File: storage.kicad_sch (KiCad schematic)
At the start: 3 parts, among them J5 Micro_SD_Card_Det1, U1 MIMX8MM6DVTLZAA, U15 W25Q32JVZP

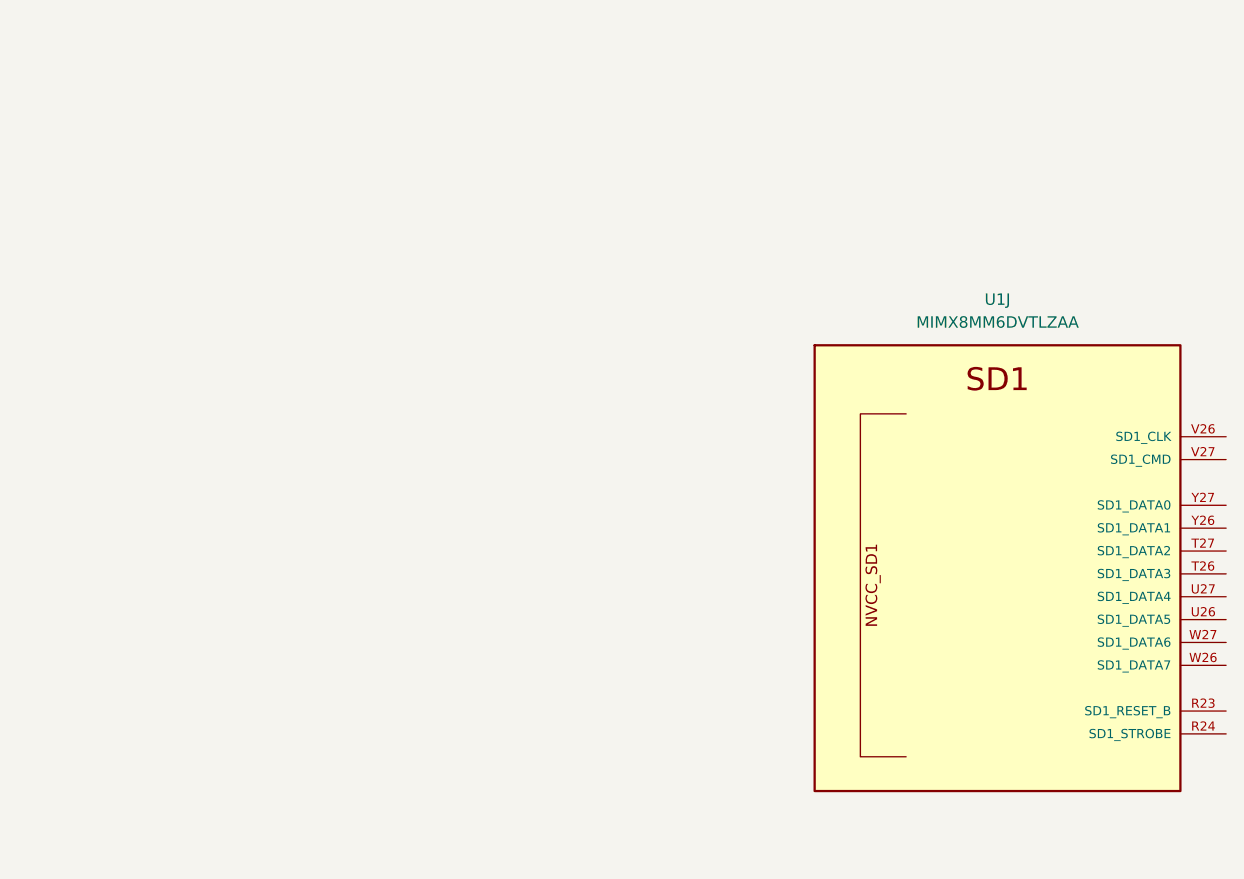
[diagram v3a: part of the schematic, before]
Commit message: enet sch done, other misc sch work
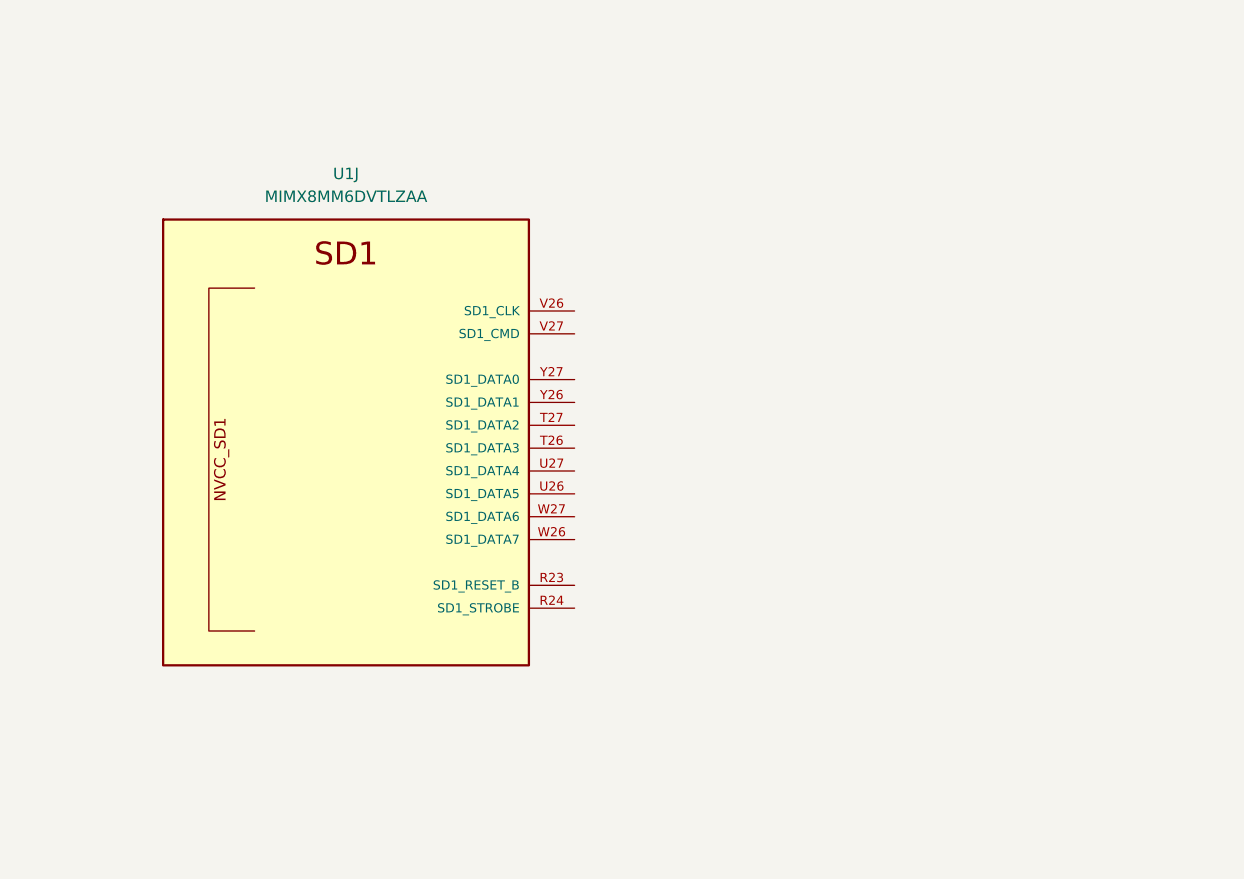
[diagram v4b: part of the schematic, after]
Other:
- moved on the sheet: U1J
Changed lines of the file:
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@@
     (pin "9")
   )
-  (symbol (lib_id "qsbc:MIMX8MM6DVTLZAA") (at 360.68 203.2 0) (unit 10)
+  (symbol (lib_id "qsbc:MIMX8MM6DVTLZAA") (at 288.29 189.23 0) (unit 10)
     (in_bom yes) (on_board yes) (fields_autoplaced)
-    (property "Reference" "U1" (id 0) (at 360.68 184.15 0))
-    (property "Value" "MIMX8MM6DVTLZAA" (id 1) (at 360.68 186.69 0))
-    (property "Footprint" "qsbc:SOT1967-1" (id 2) (at 364.49 393.7 0)
+    (property "Reference" "U1" (id 0) (at 288.29 170.18 0))
+    (property "Value" "MIMX8MM6DVTLZAA" (id 1) (at 288.29 172.72 0))
+    (property "Footprint" "qsbc:SOT1967-1" (id 2) (at 292.1 379.73 0)
       (effects (font (size 1.27 1.27)) (justify left bottom) hide)
     )
-    (property "Datasheet" "https://www.nxp.com/docs/en/data-sheet/IMX8MMCEC.pdf" (id 3) (at 361.95 397.51 0)
+    (property "Datasheet" "https://www.nxp.com/docs/en/data-sheet/IMX8MMCEC.pdf" (id 3) (at 289.56 383.54 0)
       (effects (font (size 1.27 1.27)) (justify left bottom) hide)
     )

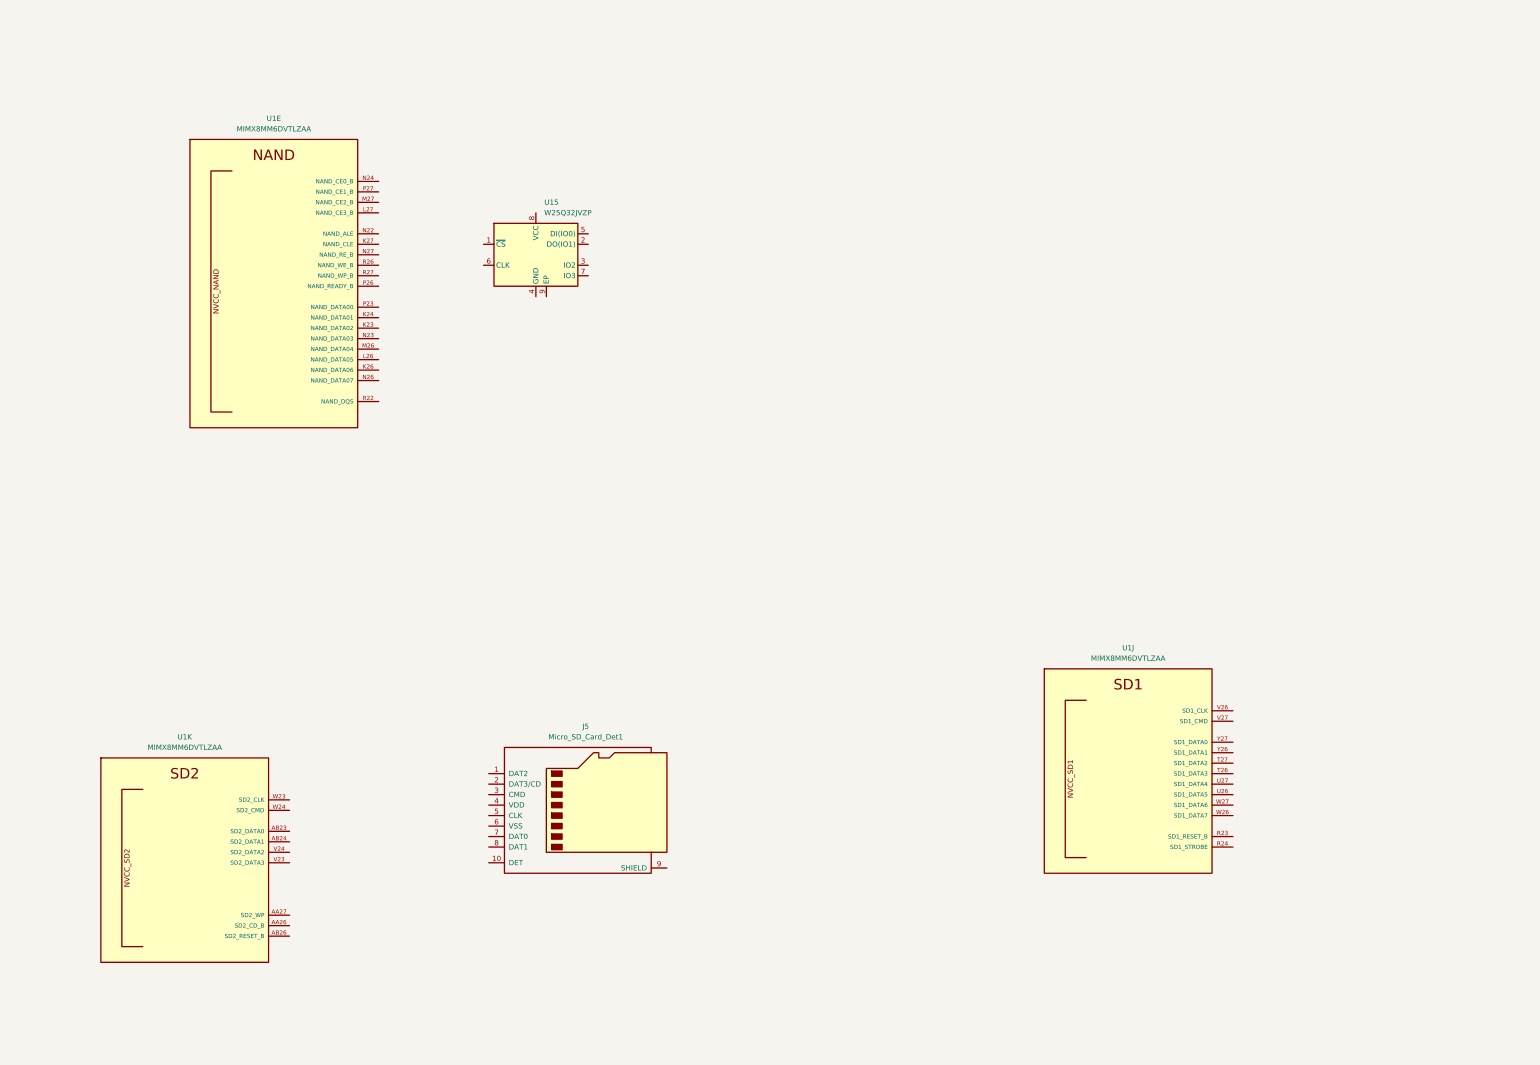
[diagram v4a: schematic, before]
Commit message: storage done, peri work, misc fixes
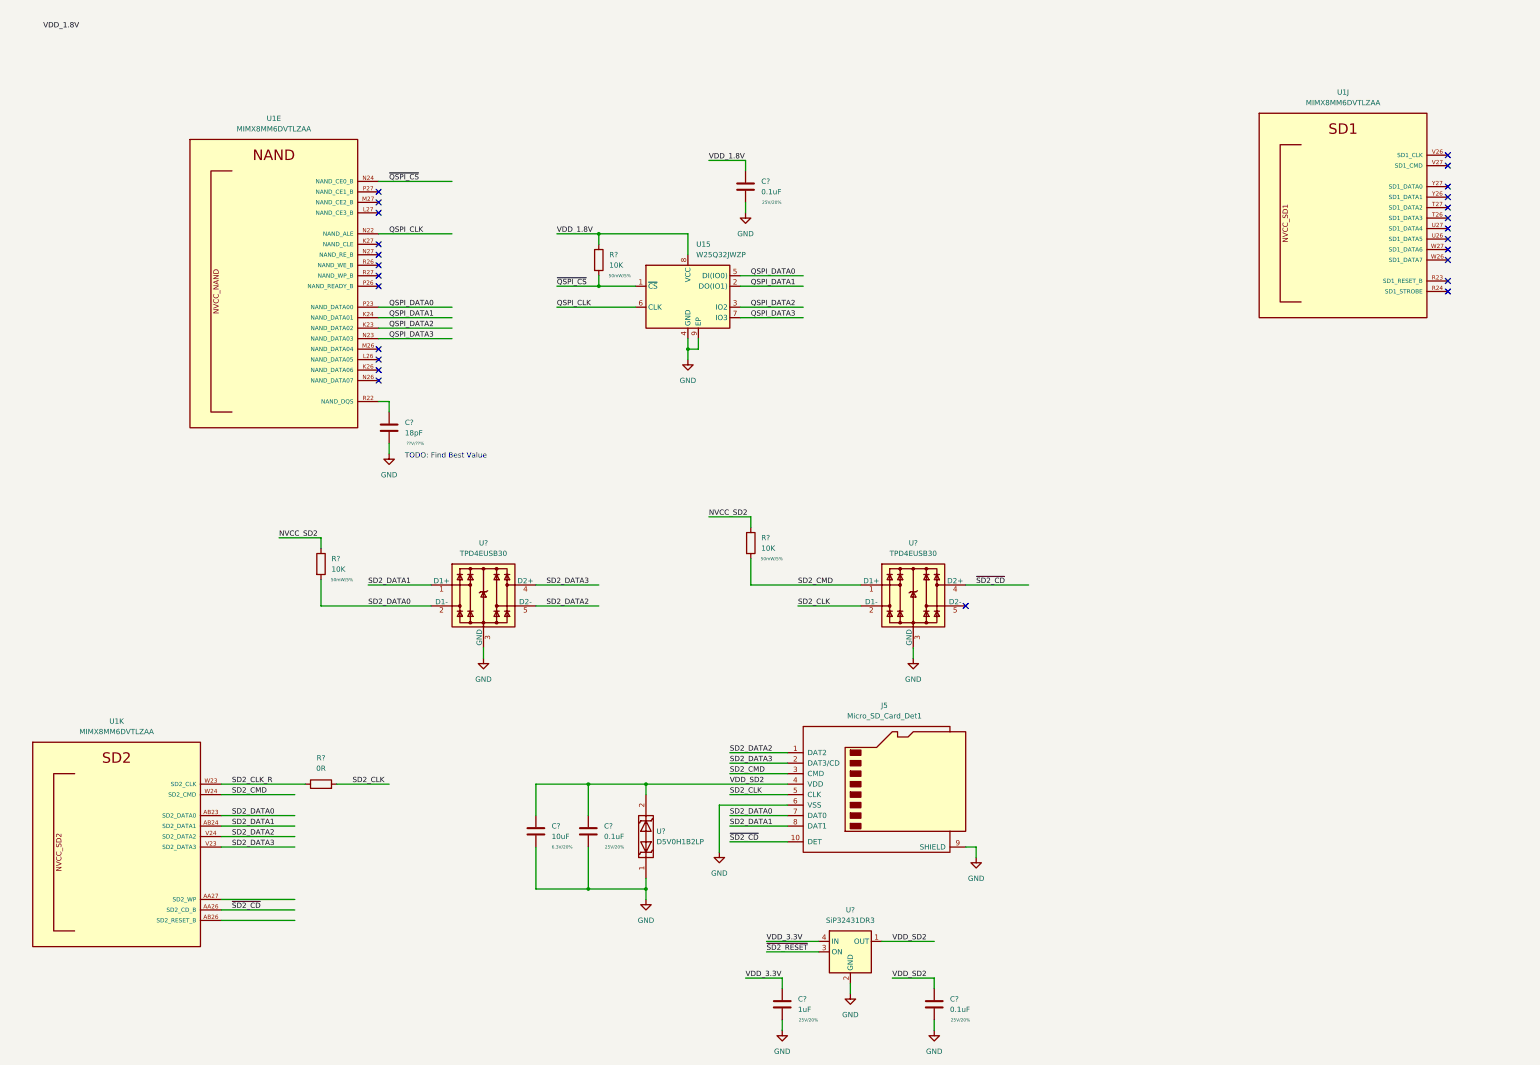
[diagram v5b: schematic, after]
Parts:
- added C?: 10uF, Capacitor_SMD:C_0603_1608Metric, symbol Device:C
- added C?: 1uF, Capacitor_SMD:C_0402_1005Metric, symbol Device:C
- added C? (x3): 0.1uF, Capacitor_SMD:C_0402_1005Metric, symbol Device:C
- added C?: 18pF, Capacitor_SMD:C_0402_1005Metric, symbol Device:C
- added R?: 0R, Resistor_SMD:R_0402_1005Metric, symbol Device:R
- added R? (x3): 10K, Resistor_SMD:R_0402_1005Metric, symbol Device:R
- added U? (x2): TPD4EUSB30, Package_SON:USON-10_2.5x1.0mm_P0.5mm, symbol qsbc:TPD4EUSB30
- added U?: D5V0H1B2LP, symbol qsbc:D5V0H1B2LP
- added U?: SiP32431DR3, Package_TO_SOT_SMD:SOT-363_SC-70-6, symbol Power_Management:SiP32431DR3
- U15: value W25Q32JVZP -> W25Q32JWZP
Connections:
- net SD2_DATA2: now reaches J5.1 (DAT2)
- net SD2_DATA2: now also U1.V24 (SD2_DATA2), U?.5 (D2-), U?.6
- net ~{SD2_CD}: now reaches J5.10 (DET)
- net ~{SD2_CD}: now also U1.AA26 (SD2_CD_B), U?.4 (D2+), U?.7
- net SD2_DATA3: now reaches J5.2 (DAT3/CD)
- net SD2_DATA3: now also U1.V23 (SD2_DATA3), U?.4 (D2+), U?.7
- net SD2_CMD: now reaches J5.3 (CMD)
- net SD2_CMD: now also U1.W24 (SD2_CMD), R?.2, U?.1 (D1+), U?.10
- net VDD_SD2: now reaches J5.4 (VDD)
- net VDD_SD2: now also C?.1, C?.1, C?.1, U?.1 (OUT), U?.2
- net SD2_CLK: now reaches J5.5 (CLK)
- net SD2_CLK: now also R?.2, U?.2 (D1-), U?.9
- net GND: now reaches J5.6 (VSS)
- net GND: now also J5.9 (SHIELD), U15.4 (GND), U15.9 (EP), C?.2, C?.2, C?.2, C?.2, C?.2, C?.2, U?.1, U?.2 (GND), U?.3 (GND), U?.3 (GND), U?.5 (GND), U?.8 (GND), U?.8 (GND)
- net SD2_DATA0: now reaches J5.7 (DAT0)
- net SD2_DATA0: now also U1.AB23 (SD2_DATA0), R?.2, U?.2 (D1-), U?.9
- net SD2_DATA1: now reaches J5.8 (DAT1)
- net SD2_DATA1: now also U1.AB24 (SD2_DATA1), U?.1 (D1+), U?.10
- net ~{QSPI_CS}: now reaches U15.1 (~{CS})
- net ~{QSPI_CS}: now also U1.N24 (NAND_CE0_B), R?.2
- net QSPI_DATA1: now reaches U15.2 (DO(IO1))
- net QSPI_DATA1: now also U1.K24 (NAND_DATA01)
- net QSPI_DATA2: now reaches U15.3 (IO2)
- net QSPI_DATA2: now also U1.K23 (NAND_DATA02)
- net QSPI_DATA0: now reaches U15.5 (DI(IO0))
- net QSPI_DATA0: now also U1.P23 (NAND_DATA00)
- net QSPI_CLK: now reaches U15.6 (CLK)
- net QSPI_CLK: now also U1.N22 (NAND_ALE)
- net QSPI_DATA3: now reaches U15.7 (IO3)
- net QSPI_DATA3: now also U1.N23 (NAND_DATA03)
- net VDD_1.8V: now reaches U15.8 (VCC)
- net VDD_1.8V: now also C?.1, R?.1
- net at U1.R22 (NAND_DQS): now also C?.1
- net SD2_CLK_R: now reaches U1.W23 (SD2_CLK)
- net SD2_CLK_R: now also R?.1
- new net: U?.5 (D2-), U?.6
- new net NVCC_SD2: R?.1, R?.1
- new net VDD_3.3V: C?.1, U?.4 (IN)
- new net ~{SD2_RESET}: U?.3 (ON)
- no-connect marks 0 -> 25
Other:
- note added: "TODO: Find Best Value"
- moved on the sheet: J5, U15, U1J, U1K

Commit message: ddr: add dual die support, misc work
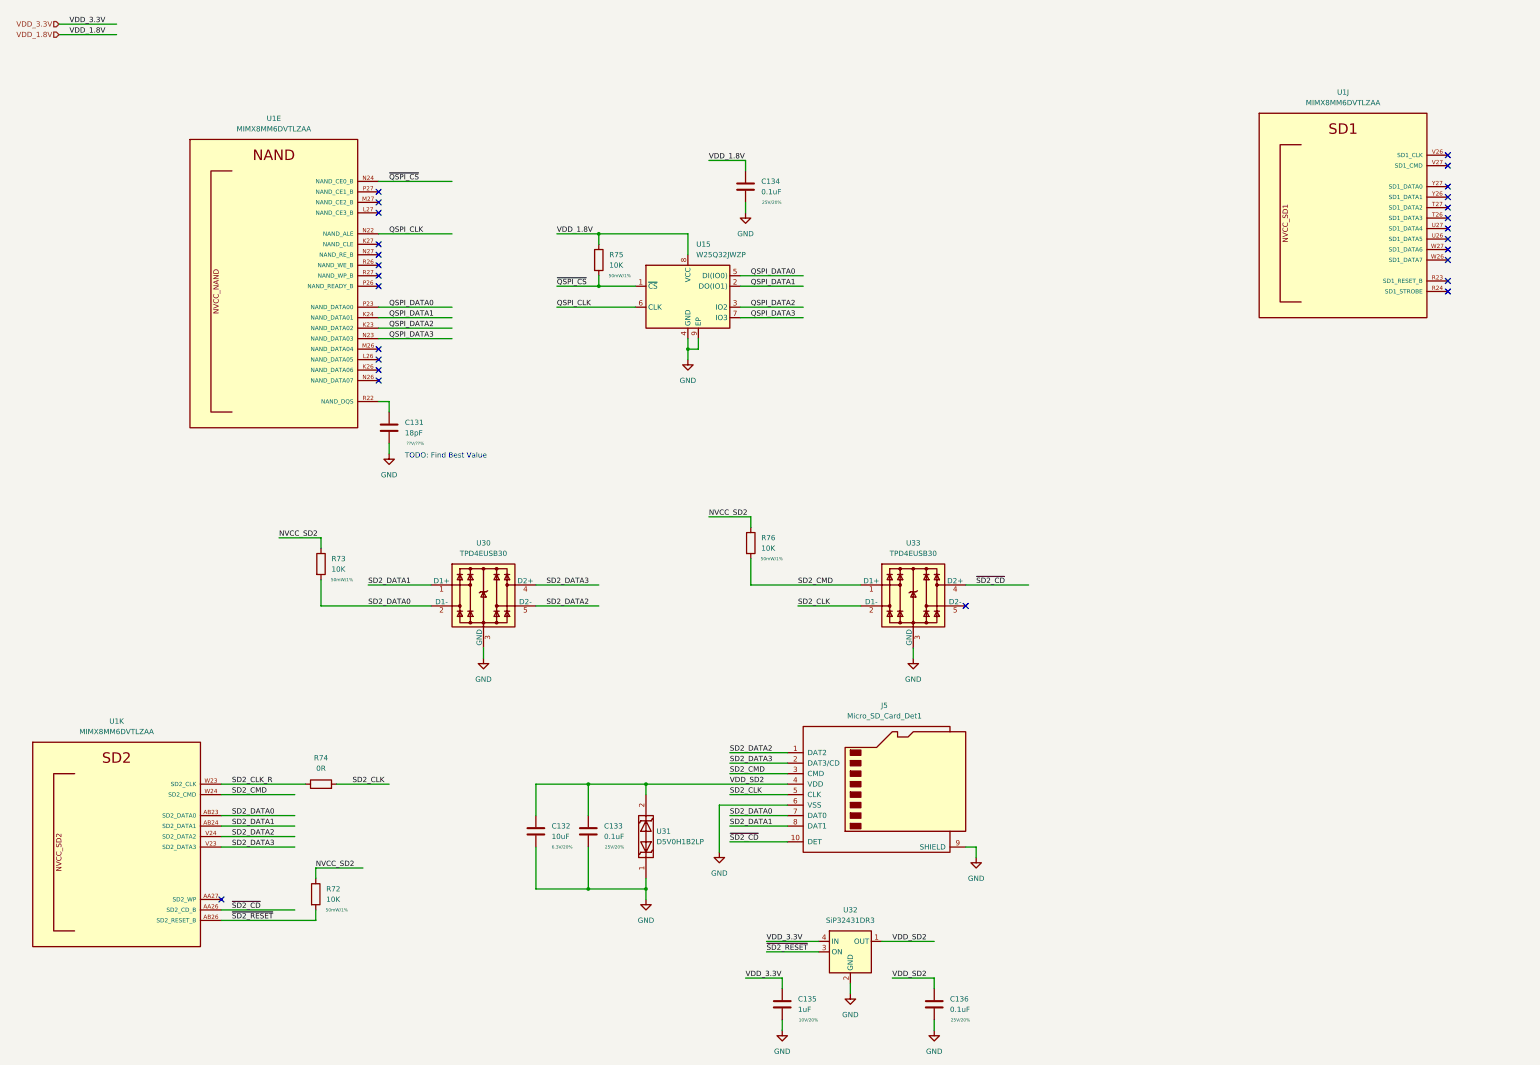
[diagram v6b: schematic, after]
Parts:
- added R72: 10K, Resistor_SMD:R_0402_1005Metric, symbol Device:R
- C132: renamed from C?; footprint Capacitor_SMD:C_0603_1608Metric -> Capacitor_SMD:C_0402_1005Metric
- C135: renamed from C?; Rating 25V/20% -> 10V/20%
- J5: footprint (none) -> qsbc:GCT_MEM2051-00-195-00-A_REVC
- R73, R75, R76: renamed from R?; Rating 50mW/5% -> 50mW/1%
- U31: renamed from U?; footprint (none) -> qsbc:DFN100X60X45-2N
- gave numbers to parts that had none: 8
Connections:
- net NVCC_SD2: now also R72.1
- net ~{SD2_RESET}: now also U1.AB26 (SD2_RESET_B), R72.2
- no-connect marks 25 -> 26
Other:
- company: (none) -> Q-LAB
- title: (none) -> QSBC
